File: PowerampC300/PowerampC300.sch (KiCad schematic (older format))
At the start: 109 parts, among them J1 Conn_01x02, J2 Conn_01x02, J3 Conn_01x02, J4 Conn_01x01, J5 Conn_01x01, J6 Conn_01x01, J7 Conn_01x01, J8 Conn_01x02, J9 Conn_Coaxial, Q1 2N5551, Q10 MJE15033, Q11 MJE15032, Q12 MJE15032, Q13 2N5551, Q14 2N5401, Q15 MJE15032, Q16 MJE15033, Q17 MJL3281A, Q18 MJL1302A, Q19 MJL3281A, Q2 2N5551, Q20 MJL1302A, Q21 MJL3281A, Q22 MJL1302A, Q23 MJL3281A, Q24 MJL1302A, Q3 2N5401, Q4 2N5401, Q5 2N5551, Q6 2N5551, Q7 2N5551, Q8 2N5401, Q9 2N5401

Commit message: JLCPCB order 2020-09-21
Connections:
- net GND: now also C11.1; no longer R41.1
- net at C6.2, D5.2 (A), D6.1 (K)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: now also R41.2; no longer C11.2
- new net: C11.2, R41.1
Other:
- moved on the sheet: C11, R41
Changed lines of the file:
@@
 L C_Small C11
 U 1 1 5F3C6684
-P 9450 4400
-F 0 "C11" V 9300 4350 50  0000 L CNN
-F 1 "0.1 uF" V 9550 4300 50  0000 L CNN
-F 2 "Capacitors_THT:C_Axial_L3.8mm_D2.6mm_P10.00mm_Horizontal" H 9450 4400 50  0001 C CNN
-F 3 "" H 9450 4400 50  0001 C CNN
-F 4 "C390130" V 9450 4400 60  0001 C CNN "LCSC"
-	1    9450 4400
+P 9450 4700
+F 0 "C11" V 9300 4650 50  0000 L CNN
+F 1 "0.1 uF" V 9550 4600 50  0000 L CNN
+F 2 "Capacitors_THT:C_Axial_L3.8mm_D2.6mm_P10.00mm_Horizontal" H 9450 4700 50  0001 C CNN
+F 3 "" H 9450 4700 50  0001 C CNN
+F 4 "C390130" V 9450 4700 60  0001 C CNN "LCSC"
+	1    9450 4700
 	-1   0    0    1
 $EndComp
@@
 L R R41
 U 1 1 5F3C6B8C
-P 9450 4700
-F 0 "R41" V 9530 4700 50  0000 C CNN
-F 1 "4R7" V 9450 4700 50  0000 C CNN
-F 2 "Resistors_THT:R_Axial_DIN0309_L9.0mm_D3.2mm_P12.70mm_Horizontal" V 9380 4700 50  0001 C CNN
-F 3 "" H 9450 4700 50  0001 C CNN
-F 4 "C57725" V 9450 4700 60  0001 C CNN "LCSC"
-	1    9450 4700
+P 9450 4400
+F 0 "R41" V 9530 4400 50  0000 C CNN
+F 1 "4R7" V 9450 4400 50  0000 C CNN
+F 2 "Resistors_THT:R_Axial_DIN0309_L9.0mm_D3.2mm_P12.70mm_Horizontal" V 9380 4400 50  0001 C CNN
+F 3 "" H 9450 4400 50  0001 C CNN
+F 4 "C57725" V 9450 4400 60  0001 C CNN "LCSC"
+	1    9450 4400
 	-1   0    0    1
 $EndComp
@@
 Connection ~ 8250 6150
 Wire Wire Line
-	9450 4900 9450 4850
-Wire Wire Line
-	9450 4550 9450 4500
+	9450 4900 9450 4800
 Wire Wire Line
 	8950 5000 8950 6150
@@
 Connection ~ 8900 2350
 Wire Wire Line
-	9450 3950 9450 4300
+	9450 3950 9450 4250
 Connection ~ 9450 4200
 Connection ~ 9150 5600
@@
 Wire Wire Line
 	3250 4200 3250 4400
+Wire Wire Line
+	9450 4550 9450 4600
 $EndSCHEMATC

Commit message: Working design 2020-10-12
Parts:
- removed Q9: 2N5401, TO_SOT_Packages_THT:TO-92_Inline_Wide, symbol Q_PNP_EBC
- removed R18: 330R, Resistors_THT:R_Axial_DIN0207_L6.3mm_D2.5mm_P7.62mm_Horizontal, symbol R
- removed R20: 27R, Resistors_THT:R_Axial_DIN0207_L6.3mm_D2.5mm_P7.62mm_Horizontal, symbol R
- added R43: 10k, Resistors_THT:R_Axial_DIN0309_L9.0mm_D3.2mm_P12.70mm_Horizontal, symbol R
- C3: value 220 pF -> 150 pF
- C9: value 100 pF -> 150 pF
- R19: value 10R -> 33R; footprint Resistors_THT:R_Axial_DIN0207_L6.3mm_D2.5mm_P7.62mm_Horizontal -> Resistors_THT:R_Axial_DIN0309_L9.0mm_D3.2mm_P12.70mm_Horizontal; LCSC C176452 -> C176446
- R23: value 150R -> 100R
- R5: value 620R -> 1k
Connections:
- net GND: now also R43.1
- net at C6.2, D5.2 (A), D6.1 (K)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: now also R43.2
- net at R19.1: now also Q10.3 (E)
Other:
- moved on the sheet: J2, L1, Q10, R42

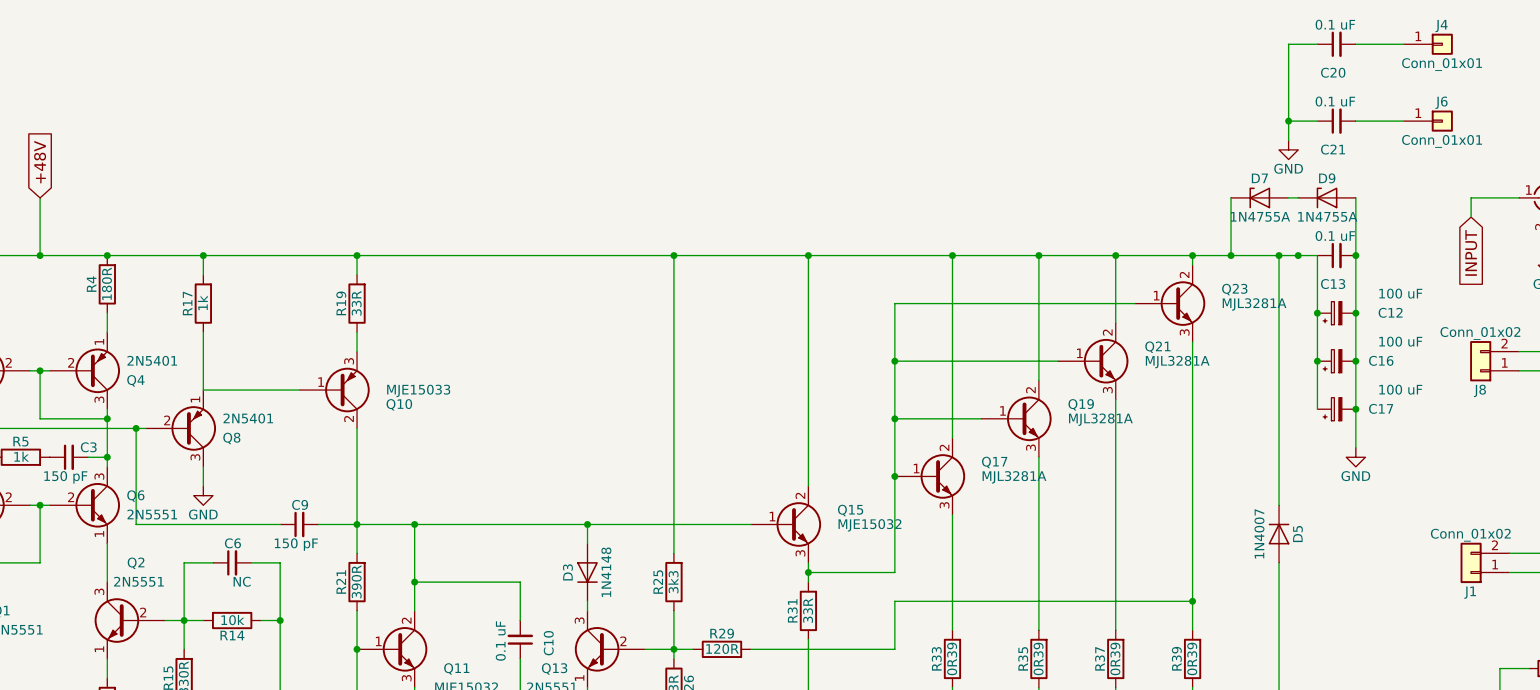
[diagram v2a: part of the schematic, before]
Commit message: Changed grounding and star layout
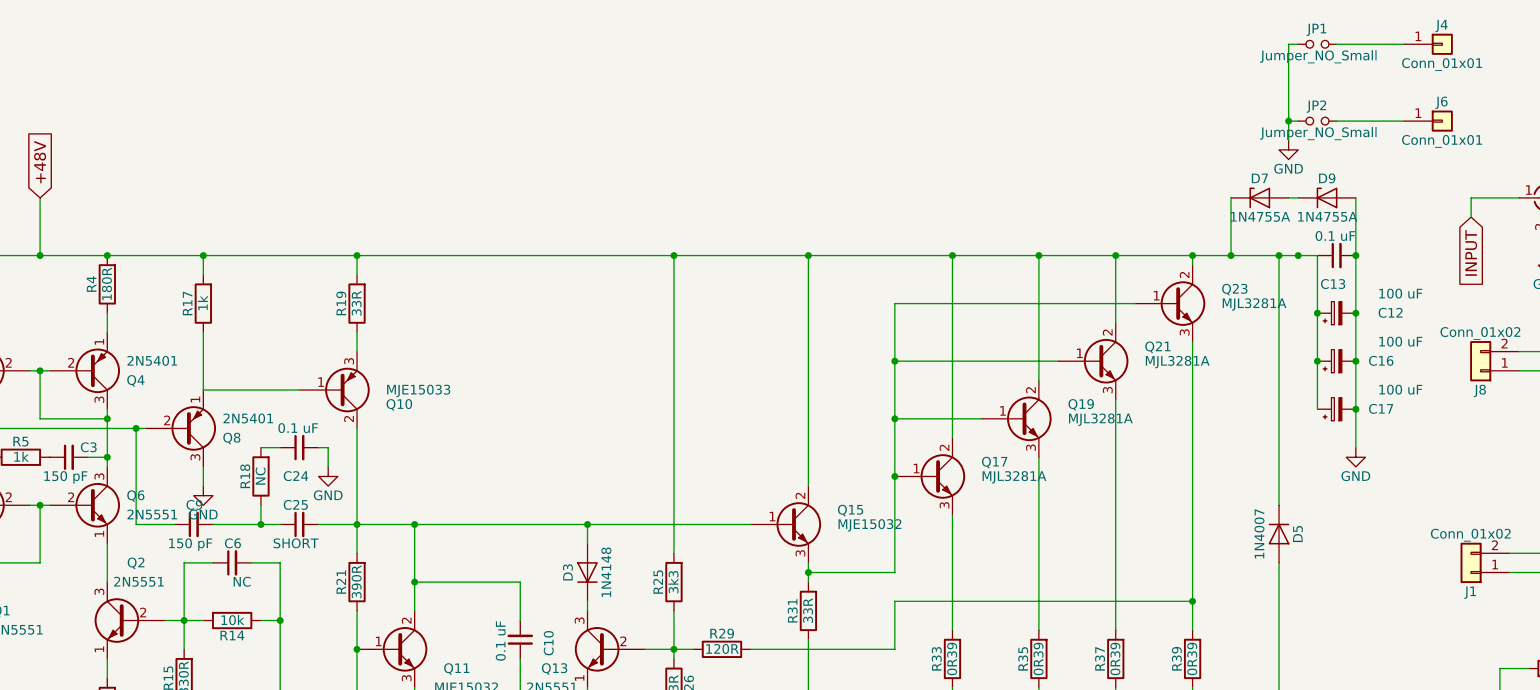
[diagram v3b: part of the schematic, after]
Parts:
- removed C20, C21: 0.1 uF, Capacitors_THT:C_Disc_D5.0mm_W2.5mm_P5.00mm, symbol C_Small
- added C24: 0.1 uF, Capacitors_THT:C_Axial_L3.8mm_D2.6mm_P10.00mm_Horizontal, symbol C_Small
- added C25: SHORT, Capacitors_THT:C_Disc_D5.0mm_W2.5mm_P5.00mm, symbol C_Small
- added JP1, JP2: Jumper_NO_Small, Pin_Headers:Pin_Header_Straight_1x02_Pitch2.54mm, symbol Jumper_NO_Small
- added R18: NC, Resistors_THT:R_Axial_DIN0207_L6.3mm_D2.5mm_P7.62mm_Horizontal, symbol R
- Q17, Q18, Q19, Q20, Q21, Q22, Q23, Q24: footprint poweramp:TO-264_Vertical_w_pads -> TO_SOT_Packages_THT:TO-264_Vertical
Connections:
- net GND: now also C24.2, JP1.1, JP2.1
- net at C10.2, D3.2 (A), Q10.2 (C)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: now also C25.2; no longer C9.2
- net at J4.1 (Pin_1): now also JP1.2
- net at J6.1 (Pin_1): now also JP2.2
- new net: C25.1, C9.2, R18.1
- new net: C24.1, R18.2
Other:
- moved on the sheet: C9

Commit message: Moved Q1 and Q2 together
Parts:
- Q17, Q18, Q19, Q20, Q21, Q22, Q23, Q24: footprint TO_SOT_Packages_THT:TO-264_Vertical -> poweramp:TO-264_Vertical_w_pads
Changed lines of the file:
@@
 F 0 "Q17" H 7150 3025 50  0000 L CNN
 F 1 "MJL3281A" H 7150 2950 50  0000 L CNN
-F 2 "TO_SOT_Packages_THT:TO-264_Vertical" H 7150 2875 50  0001 L CIN
+F 2 "poweramp:TO-264_Vertical_w_pads" H 7150 2875 50  0001 L CIN
 F 3 "" H 6900 2950 50  0001 L CNN
 F 4 "C327498" H 6900 2950 60  0001 C CNN "LCSC"
@@
 F 0 "Q18" H 7150 5025 50  0000 L CNN
 F 1 "MJL1302A" H 7150 4950 50  0000 L CNN
-F 2 "TO_SOT_Packages_THT:TO-264_Vertical" H 7150 4875 50  0001 L CIN
+F 2 "poweramp:TO-264_Vertical_w_pads" H 7150 4875 50  0001 L CIN
 F 3 "" H 6900 4950 50  0001 L CNN
 F 4 "C327497" H 6900 4950 60  0001 C CNN "LCSC"
@@
 F 0 "Q19" H 7600 2725 50  0000 L CNN
 F 1 "MJL3281A" H 7600 2650 50  0000 L CNN
-F 2 "TO_SOT_Packages_THT:TO-264_Vertical" H 7600 2575 50  0001 L CIN
+F 2 "poweramp:TO-264_Vertical_w_pads" H 7600 2575 50  0001 L CIN
 F 3 "" H 7350 2650 50  0001 L CNN
 F 4 "C327498" H 7350 2650 60  0001 C CNN "LCSC"
@@
 F 0 "Q21" H 8000 2425 50  0000 L CNN
 F 1 "MJL3281A" H 8000 2350 50  0000 L CNN
-F 2 "TO_SOT_Packages_THT:TO-264_Vertical" H 8000 2275 50  0001 L CIN
+F 2 "poweramp:TO-264_Vertical_w_pads" H 8000 2275 50  0001 L CIN
 F 3 "" H 7750 2350 50  0001 L CNN
 F 4 "C327498" H 7750 2350 60  0001 C CNN "LCSC'"
@@
 F 0 "Q23" H 8400 2125 50  0000 L CNN
 F 1 "MJL3281A" H 8400 2050 50  0000 L CNN
-F 2 "TO_SOT_Packages_THT:TO-264_Vertical" H 8400 1975 50  0001 L CIN
+F 2 "poweramp:TO-264_Vertical_w_pads" H 8400 1975 50  0001 L CIN
 F 3 "" H 8150 2050 50  0001 L CNN
 F 4 "C327498" H 8150 2050 60  0001 C CNN "LCSC"
@@
 F 0 "Q20" H 7600 5325 50  0000 L CNN
 F 1 "MJL1302A" H 7600 5250 50  0000 L CNN
-F 2 "TO_SOT_Packages_THT:TO-264_Vertical" H 7600 5175 50  0001 L CIN
+F 2 "poweramp:TO-264_Vertical_w_pads" H 7600 5175 50  0001 L CIN
 F 3 "" H 7350 5250 50  0001 L CNN
 F 4 "C327497" H 7350 5250 60  0001 C CNN "LCSC"
@@
 F 0 "Q22" H 8000 5625 50  0000 L CNN
 F 1 "MJL1302A" H 8000 5550 50  0000 L CNN
-F 2 "TO_SOT_Packages_THT:TO-264_Vertical" H 8000 5475 50  0001 L CIN
+F 2 "poweramp:TO-264_Vertical_w_pads" H 8000 5475 50  0001 L CIN
 F 3 "" H 7750 5550 50  0001 L CNN
 F 4 "C327497" H 7750 5550 60  0001 C CNN "LCSC"
@@
 F 0 "Q24" H 8400 5875 50  0000 L CNN
 F 1 "MJL1302A" H 8400 5800 50  0000 L CNN
-F 2 "TO_SOT_Packages_THT:TO-264_Vertical" H 8400 5725 50  0001 L CIN
+F 2 "poweramp:TO-264_Vertical_w_pads" H 8400 5725 50  0001 L CIN
 F 3 "" H 8150 5800 50  0001 L CNN
 F 4 "C327497" H 8150 5800 60  0001 C CNN "LCSC"

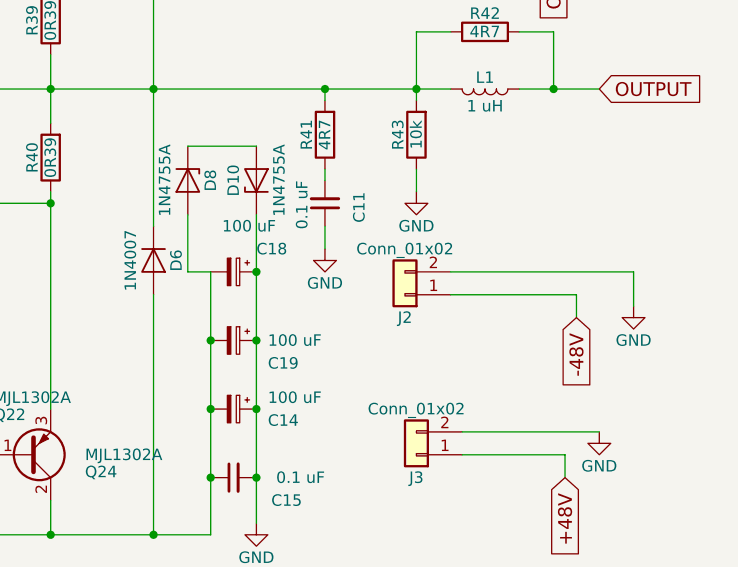
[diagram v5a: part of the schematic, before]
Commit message: Added option for spade terminal power connections
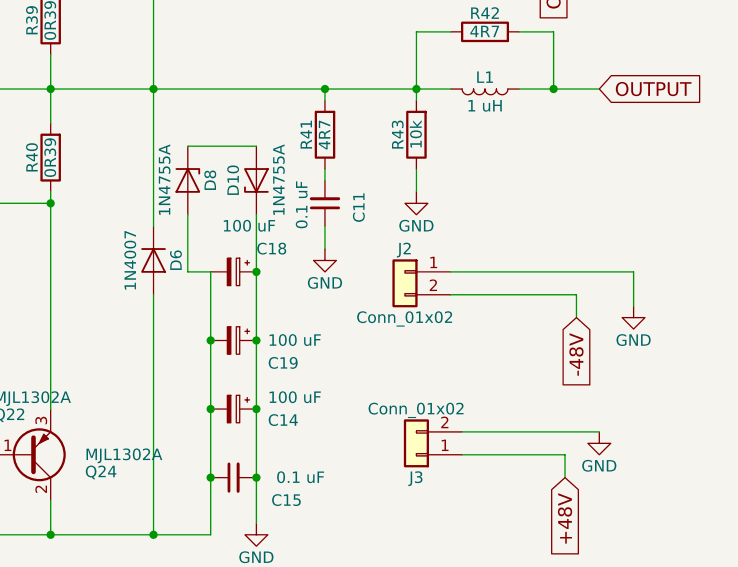
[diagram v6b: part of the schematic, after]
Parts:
- J1, J2, J3: footprint Connectors_Terminal_Blocks:TerminalBlock_bornier-2_P5.08mm -> poweramp:TerminalBlock_bornier-2_P5.08mm_with_spade
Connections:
- net -48V: now also J2.2 (Pin_2); no longer J2.1 (Pin_1)
- net GND: now also J2.1 (Pin_1); no longer J2.2 (Pin_2)
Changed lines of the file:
@@
 F 0 "J1" H 9700 3550 50  0000 C CNN
 F 1 "Conn_01x02" H 9700 3250 50  0000 C CNN
-F 2 "Connectors_Terminal_Blocks:TerminalBlock_bornier-2_P5.08mm" H 9700 3450 50  0001 C CNN
+F 2 "poweramp:TerminalBlock_bornier-2_P5.08mm_with_spade" H 9700 3450 50  0001 C CNN
 F 3 "" H 9700 3450 50  0001 C CNN
 F 4 "C395849" H 9700 3450 60  0001 C CNN "LCSC"
@@
 L Conn_01x02 J2
 U 1 1 5F3DAA81
-P 9800 5100
-F 0 "J2" H 9800 5200 50  0000 C CNN
-F 1 "Conn_01x02" H 9800 4900 50  0000 C CNN
-F 2 "Connectors_Terminal_Blocks:TerminalBlock_bornier-2_P5.08mm" H 9800 5100 50  0001 C CNN
-F 3 "" H 9800 5100 50  0001 C CNN
-F 4 "C395849" H 9800 5100 60  0001 C CNN "LCSC"
-	1    9800 5100
-	-1   0    0    1
+P 9800 5000
+F 0 "J2" H 9800 5100 50  0000 C CNN
+F 1 "Conn_01x02" H 9800 4800 50  0000 C CNN
+F 2 "poweramp:TerminalBlock_bornier-2_P5.08mm_with_spade" H 9800 5000 50  0001 C CNN
+F 3 "" H 9800 5000 50  0001 C CNN
+F 4 "C395849" H 9800 5000 60  0001 C CNN "LCSC"
+	1    9800 5000
+	-1   0    0    -1
 $EndComp
 $Comp
@@
 F 0 "J3" H 9850 5900 50  0000 C CNN
 F 1 "Conn_01x02" H 9850 5600 50  0000 C CNN
-F 2 "Connectors_Terminal_Blocks:TerminalBlock_bornier-2_P5.08mm" H 9850 5800 50  0001 C CNN
+F 2 "poweramp:TerminalBlock_bornier-2_P5.08mm_with_spade" H 9850 5800 50  0001 C CNN
 F 3 "" H 9850 5800 50  0001 C CNN
 F 4 "C395849" H 9850 5800 60  0001 C CNN "LCSC"

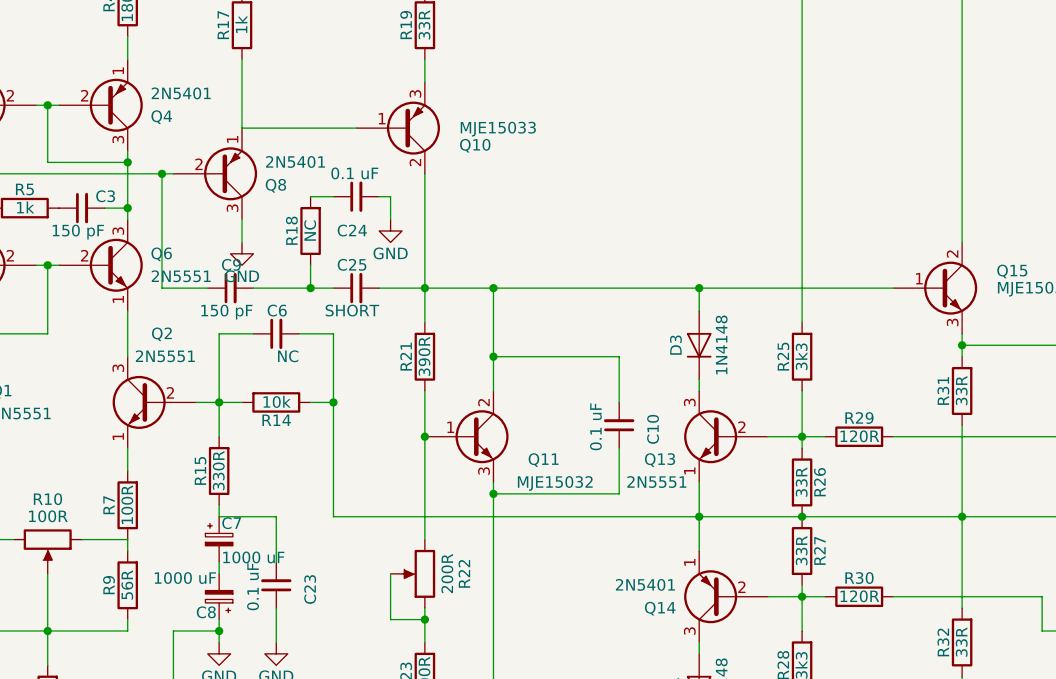
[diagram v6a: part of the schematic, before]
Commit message: Added OITPC compensation
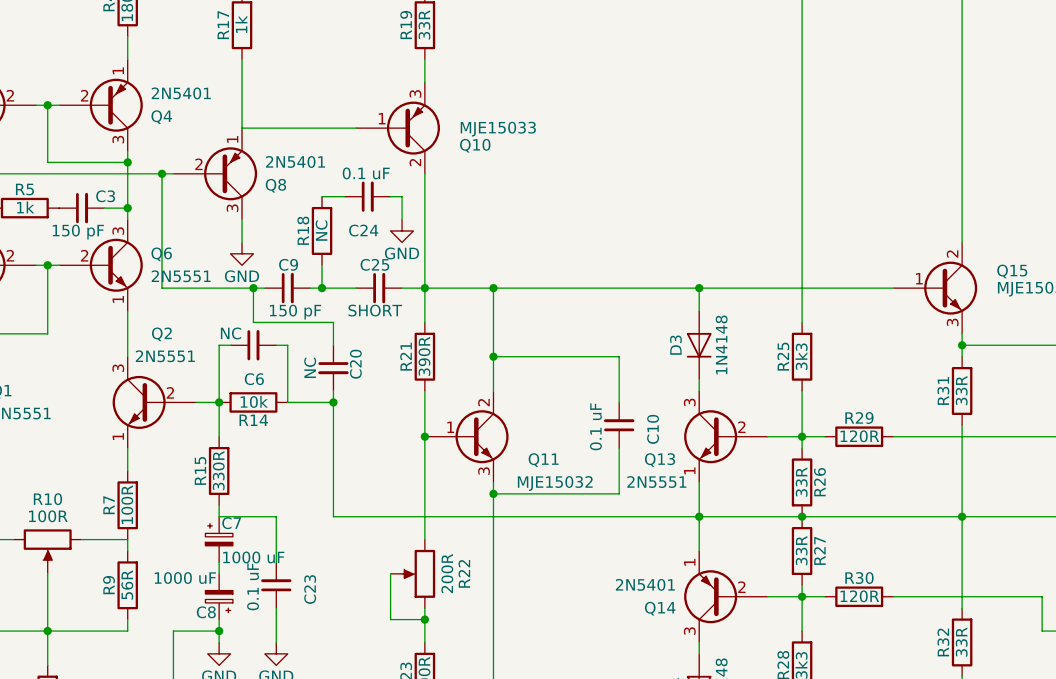
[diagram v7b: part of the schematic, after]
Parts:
- added C20: NC, Capacitors_THT:C_Disc_D5.0mm_W2.5mm_P5.00mm, symbol C_Small
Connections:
- net at C9.1, Q3.3 (C), Q5.3 (C)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: now also C20.1
- net at C6.2, D5.2 (A), D6.1 (K)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: now also C20.2
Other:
- moved on the sheet: C24, C25, C6, C9, R14, R18
